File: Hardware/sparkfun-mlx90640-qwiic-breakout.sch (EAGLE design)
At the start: 24 parts, among them J3 PTH, U1 110DEG

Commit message: updating to kit package
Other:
- note added: "v11"
- note removed: "v10"
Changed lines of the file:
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@@
 <grid distance="0.1" unitdist="inch" unit="inch" style="lines" multiple="1" display="no" altdistance="0.01" altunitdist="inch" altunit="inch"/>
 <layers>
-<layer number="1" name="Top" color="4" fill="1" visible="yes" active="no"/>
-<layer number="2" name="Route2" color="1" fill="3" visible="yes" active="no"/>
-<layer number="15" name="Route15" color="4" fill="6" visible="yes" active="no"/>
-<layer number="16" name="Bottom" color="1" fill="1" visible="yes" active="no"/>
-<layer number="17" name="Pads" color="2" fill="1" visible="yes" active="no"/>
-<layer number="18" name="Vias" color="2" fill="1" visible="yes" active="no"/>
-<layer number="19" name="Unrouted" color="6" fill="1" visible="yes" active="no"/>
-<layer number="20" name="Dimension" color="15" fill="1" visible="yes" active="no"/>
-<layer number="21" name="tPlace" color="16" fill="1" visible="yes" active="no"/>
-<layer number="22" name="bPlace" color="14" fill="1" visible="yes" active="no"/>
-<layer number="23" name="tOrigins" color="15" fill="1" visible="yes" active="no"/>
-<layer number="24" name="bOrigins" color="15" fill="1" visible="yes" active="no"/>
-<layer number="25" name="tNames" color="7" fill="1" visible="yes" active="no"/>
-<layer number="26" name="bNames" color="7" fill="1" visible="yes" active="no"/>
-<layer number="27" name="tValues" color="7" fill="1" visible="yes" active="no"/>
-<layer number="28" name="bValues" color="7" fill="1" visible="yes" active="no"/>
+<layer number="1" name="Top" color="4" fill="1" visible="no" active="no"/>
+<layer number="2" name="Route2" color="1" fill="3" visible="no" active="no"/>
+<layer number="15" name="Route15" color="4" fill="6" visible="no" active="no"/>
+<layer number="16" name="Bottom" color="1" fill="1" visible="no" active="no"/>
+<layer number="17" name="Pads" color="2" fill="1" visible="no" active="no"/>
+<layer number="18" name="Vias" color="2" fill="1" visible="no" active="no"/>
+<layer number="19" name="Unrouted" color="6" fill="1" visible="no" active="no"/>
+<layer number="20" name="Dimension" color="15" fill="1" visible="no" active="no"/>
+<layer number="21" name="tPlace" color="16" fill="1" visible="no" active="no"/>
+<layer number="22" name="bPlace" color="14" fill="1" visible="no" active="no"/>
+<layer number="23" name="tOrigins" color="15" fill="1" visible="no" active="no"/>
+<layer number="24" name="bOrigins" color="15" fill="1" visible="no" active="no"/>
+<layer number="25" name="tNames" color="7" fill="1" visible="no" active="no"/>
+<layer number="26" name="bNames" color="7" fill="1" visible="no" active="no"/>
+<layer number="27" name="tValues" color="7" fill="1" visible="no" active="no"/>
+<layer number="28" name="bValues" color="7" fill="1" visible="no" active="no"/>
 <layer number="29" name="tStop" color="7" fill="3" visible="no" active="no"/>
 <layer number="30" name="bStop" color="7" fill="6" visible="no" active="no"/>
@@
 <layer number="35" name="tGlue" color="7" fill="4" visible="no" active="no"/>
 <layer number="36" name="bGlue" color="7" fill="5" visible="no" active="no"/>
-<layer number="37" name="tTest" color="7" fill="1" visible="yes" active="no"/>
-<layer number="38" name="bTest" color="7" fill="1" visible="yes" active="no"/>
+<layer number="37" name="tTest" color="7" fill="1" visible="no" active="no"/>
+<layer number="38" name="bTest" color="7" fill="1" visible="no" active="no"/>
 <layer number="39" name="tKeepout" color="4" fill="11" visible="no" active="no"/>
 <layer number="40" name="bKeepout" color="1" fill="11" visible="no" active="no"/>
@@
 <layer number="44" name="Drills" color="7" fill="1" visible="no" active="no"/>
 <layer number="45" name="Holes" color="7" fill="1" visible="no" active="no"/>
-<layer number="46" name="Milling" color="3" fill="1" visible="yes" active="no"/>
-<layer number="47" name="Measures" color="7" fill="1" visible="yes" active="no"/>
-<layer number="48" name="Document" color="7" fill="1" visible="yes" active="no"/>
-<layer number="49" name="Reference" color="7" fill="1" visible="yes" active="no"/>
-<layer number="50" name="dxf" color="7" fill="1" visible="yes" active="no"/>
-<layer number="51" name="tDocu" color="6" fill="1" visible="yes" active="no"/>
-<layer number="52" name="bDocu" color="7" fill="1" visible="yes" active="no"/>
-<layer number="53" name="tGND_GNDA" color="7" fill="9" visible="yes" active="no"/>
-<layer number="54" name="bGND_GNDA" color="1" fill="9" visible="yes" active="no"/>
-<layer number="56" name="wert" color="7" fill="1" visible="yes" active="no"/>
-<layer number="57" name="tCAD" color="7" fill="1" visible="yes" active="no"/>
-<layer number="59" name="tCarbon" color="7" fill="1" visible="yes" active="no"/>
-<layer number="60" name="bCarbon" color="7" fill="1" visible="yes" active="no"/>
+<layer number="46" name="Milling" color="3" fill="1" visible="no" active="no"/>
+<layer number="47" name="Measures" color="7" fill="1" visible="no" active="no"/>
+<layer number="48" name="Document" color="7" fill="1" visible="no" active="no"/>
+<layer number="49" name="Reference" color="7" fill="1" visible="no" active="no"/>
+<layer number="50" name="dxf" color="7" fill="1" visible="no" active="no"/>
+<layer number="51" name="tDocu" color="6" fill="1" visible="no" active="no"/>
+<layer number="52" name="bDocu" color="7" fill="1" visible="no" active="no"/>
+<layer number="53" name="tGND_GNDA" color="7" fill="9" visible="no" active="no"/>
+<layer number="54" name="bGND_GNDA" color="1" fill="9" visible="no" active="no"/>
+<layer number="56" name="wert" color="7" fill="1" visible="no" active="no"/>
+<layer number="57" name="tCAD" color="7" fill="1" visible="no" active="no"/>
+<layer number="59" name="tCarbon" color="7" fill="1" visible="no" active="no"/>
+<layer number="60" name="bCarbon" color="7" fill="1" visible="no" active="no"/>
 <layer number="88" name="SimResults" color="9" fill="1" visible="yes" active="yes"/>
 <layer number="89" name="SimProbes" color="9" fill="1" visible="yes" active="yes"/>
@@
 <text x="165.354" y="11.43" size="2.54" layer="94" font="vector">Jim Lindblom</text>
 <text x="106.68" y="93.98" size="1.778" layer="97" font="vector">7-bit unshifted I2C Address: 0x33</text>
-<text x="236.22" y="7.62" size="2.54" layer="94" font="vector">v10</text>
+<text x="236.22" y="7.62" size="2.54" layer="94" font="vector">v11</text>
 <text x="168.656" y="7.366" size="2.54" layer="94" font="vector">Andy England</text>
 <text x="114.3" y="132.08" size="2.54" layer="95" font="vector">MLX90640</text>

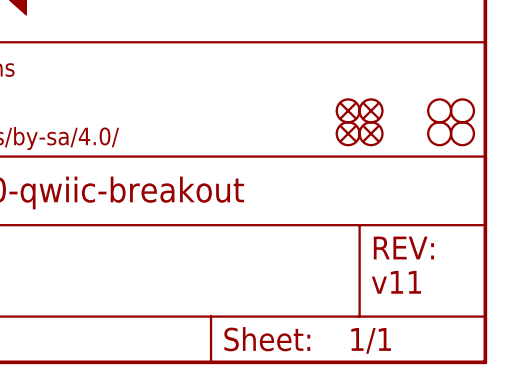
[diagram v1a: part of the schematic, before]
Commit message: fixing orientation
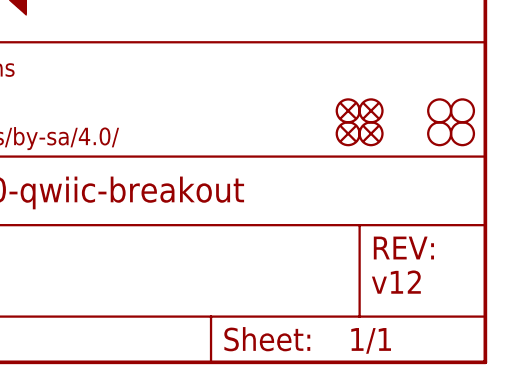
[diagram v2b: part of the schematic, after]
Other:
- note added: "v12"
- note removed: "v11"
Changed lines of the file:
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@@
 <text x="165.354" y="11.43" size="2.54" layer="94" font="vector">Jim Lindblom</text>
 <text x="106.68" y="93.98" size="1.778" layer="97" font="vector">7-bit unshifted I2C Address: 0x33</text>
-<text x="236.22" y="7.62" size="2.54" layer="94" font="vector">v11</text>
+<text x="236.22" y="7.62" size="2.54" layer="94" font="vector">v12</text>
 <text x="168.656" y="7.366" size="2.54" layer="94" font="vector">Andy England</text>
 <text x="114.3" y="132.08" size="2.54" layer="95" font="vector">MLX90640</text>
